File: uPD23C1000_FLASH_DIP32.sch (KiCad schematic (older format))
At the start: 7 parts, among them J1 uPD23C1000 / FLASH, U1 GLS29EE010 (TSOP), U2 SST39SF010 (TSOP), U3 SST39SF010 / GLS29EE010 (PLCC)

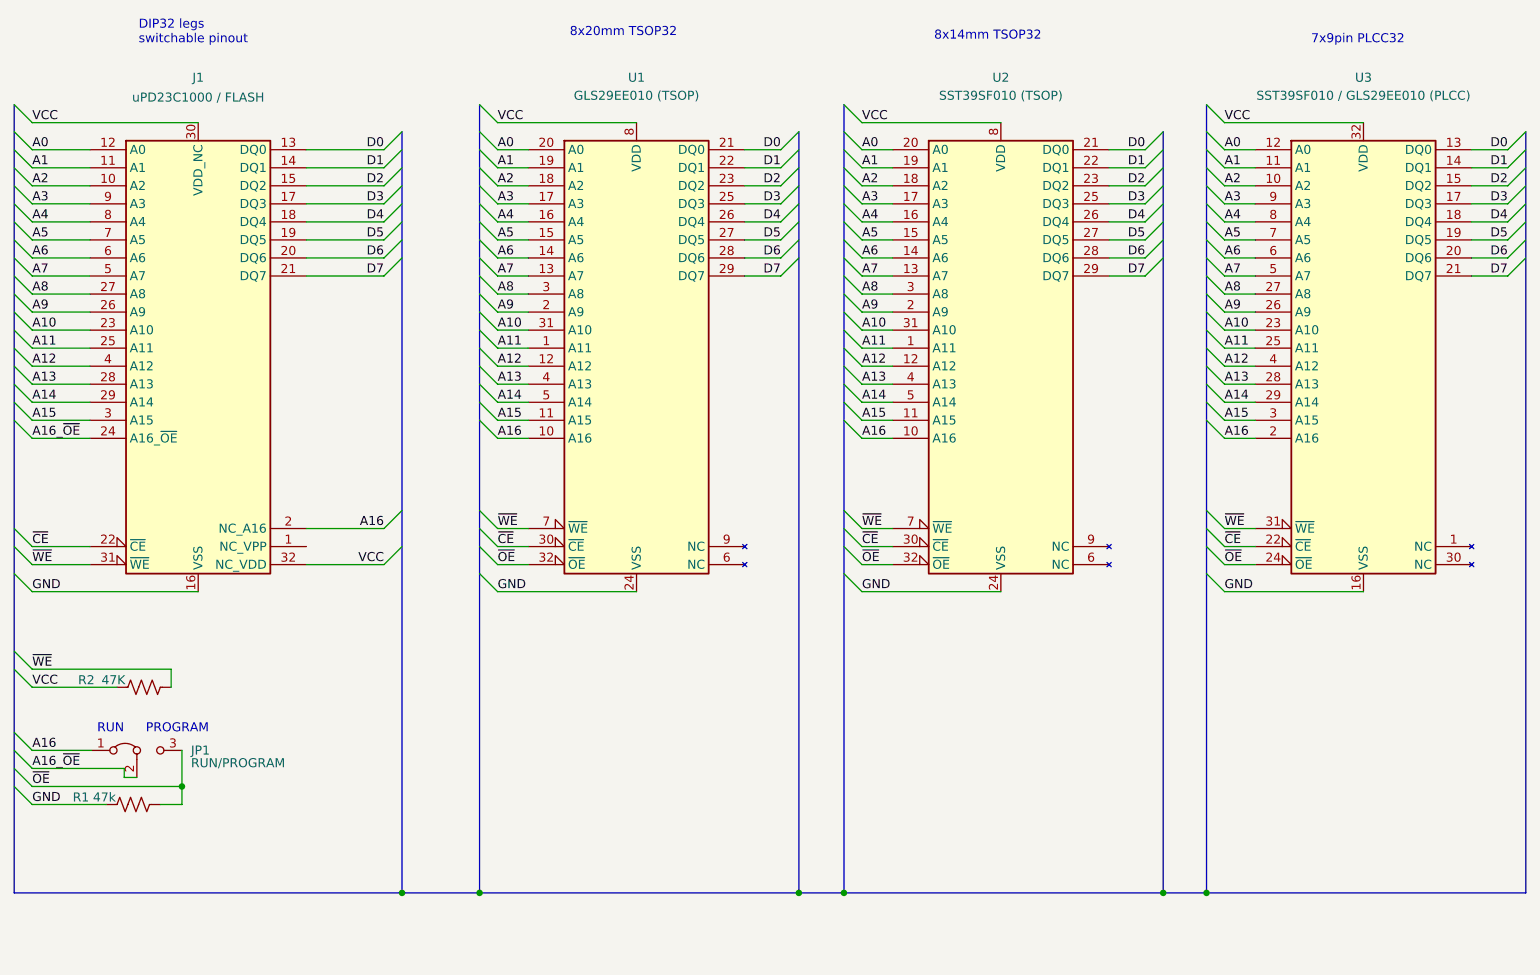
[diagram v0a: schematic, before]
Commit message: docs for FlashROM_8300, add VPP & pullup on FlashROM_8300 to support old flash, eeprom, & eprom devices.
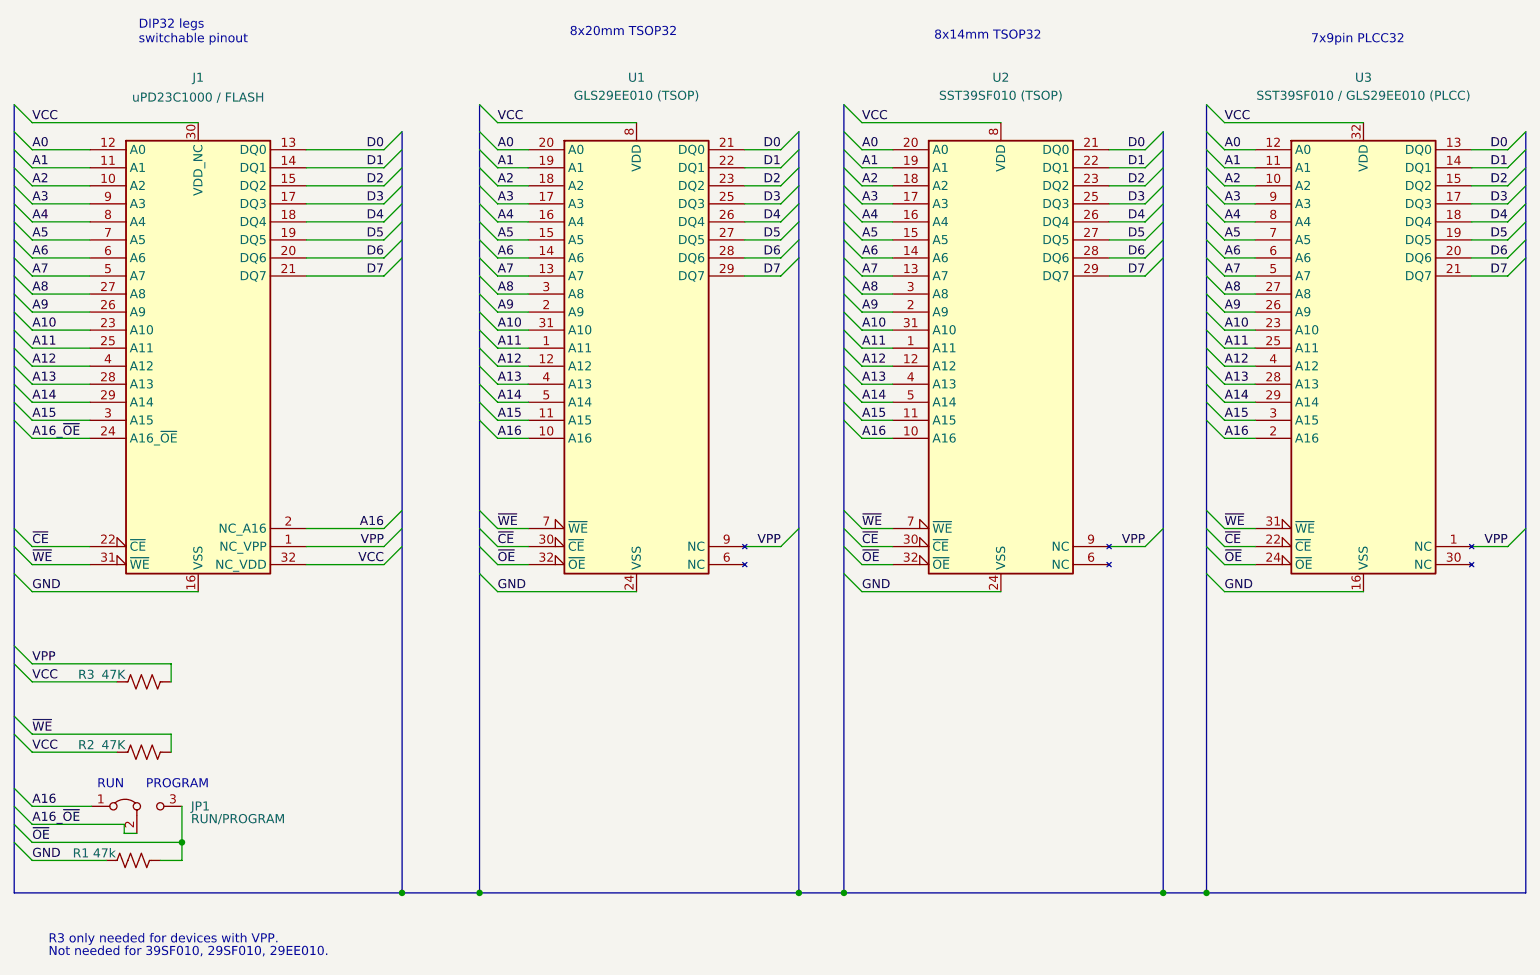
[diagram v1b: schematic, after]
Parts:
- added R3: 47K, 000_LOCAL:R_0805, symbol 000_LOCAL:R_US
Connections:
- net VCC: now also R3.2
- net VPP: now reaches J1.1 (NC_VPP)
- net VPP: now also U1.9 (NC), U2.9 (NC), U3.1 (NC), R3.1
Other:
- note added: "Not needed for 39SF010, 29SF010, 29EE010."
- note added: "R3 only needed for devices with VPP."
- moved on the sheet: JP1, R1, R2
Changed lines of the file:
@@
 Text Label 1270 3900 0    50   ~ 0
 A16_~OE
-Text Label 1270 5930 0    50   ~ 0
+Text Label 1270 6240 0    50   ~ 0
 GND
 Text Label 3850 4500 0    50   ~ 0
@@
 	3750 4400 3850 4500
 Entry Wire Line
-	1170 5830 1270 5930
+	1170 6140 1270 6240
 Entry Wire Line
 	3750 3600 3850 3700
@@
 L 000_LOCAL:R_US R1
 U 1 1 5E614D7E
-P 1830 5930
-F 0 "R1" V 1790 5640 50  0000 C CNN
-F 1 "47k" V 1790 5770 50  0000 C CNN
-F 2 "000_LOCAL:R_0805" V 1870 5920 50  0001 C CNN
-F 3 "~" H 1830 5930 50  0001 C CNN
-	1    1830 5930
+P 1830 6240
+F 0 "R1" V 1790 5950 50  0000 C CNN
+F 1 "47k" V 1790 6080 50  0000 C CNN
+F 2 "000_LOCAL:R_0805" V 1870 6230 50  0001 C CNN
+F 3 "~" H 1830 6240 50  0001 C CNN
+	1    1830 6240
 	0    1    1    0
 $EndComp
@@
 ~OE
 Entry Wire Line
-	1170 5530 1270 5630
-Text Label 1270 5630 0    50   ~ 0
+	1170 5840 1270 5940
+Text Label 1270 5940 0    50   ~ 0
 A16
 Entry Wire Line
-	1170 5080 1270 5180
-Entry Wire Line
-	1170 5180 1270 5280
-Text Label 1270 5280 0    50   ~ 0
+	1170 5440 1270 5540
+Entry Wire Line
+	1170 5540 1270 5640
+Text Label 1270 5640 0    50   ~ 0
 VCC
-Text Label 1270 5180 0    50   ~ 0
+Text Label 1270 5540 0    50   ~ 0
 ~WE
 $Comp
 L Jumper:Jumper_3_Bridged12 JP1
 U 1 1 5E634357
-P 1850 5630
-F 0 "JP1" H 2150 5630 50  0000 L CNN
-F 1 "RUN/PROGRAM" H 2150 5560 50  0000 L CNN
-F 2 "000_LOCAL:Pin_Header_Angled_1x03_Pitch2.54mm" H 1850 5630 50  0001 C CNN
-F 3 "~" H 1850 5630 50  0001 C CNN
-	1    1850 5630
+P 1850 5940
+F 0 "JP1" H 2150 5940 50  0000 L CNN
+F 1 "RUN/PROGRAM" H 2150 5870 50  0000 L CNN
+F 2 "000_LOCAL:Pin_Header_Angled_1x03_Pitch2.54mm" H 1850 5940 50  0001 C CNN
+F 3 "~" H 1850 5940 50  0001 C CNN
+	1    1850 5940
 	1    0    0    -1
 $EndComp
 Wire Wire Line
-	1270 5630 1600 5630
-Entry Wire Line
-	1170 5630 1270 5730
-Entry Wire Line
-	1170 5730 1270 5830
-Wire Wire Line
-	1850 5780 1780 5780
-Wire Wire Line
-	1780 5780 1780 5730
-Wire Wire Line
-	1780 5730 1270 5730
-Wire Wire Line
-	1270 5830 2100 5830
-Wire Wire Line
-	2100 5830 2100 5630
-Text Label 1270 5830 0    50   ~ 0
+	1270 5940 1600 5940
+Entry Wire Line
+	1170 5940 1270 6040
+Entry Wire Line
+	1170 6040 1270 6140
+Wire Wire Line
+	1850 6090 1780 6090
+Wire Wire Line
+	1780 6090 1780 6040
+Wire Wire Line
+	1780 6040 1270 6040
+Wire Wire Line
+	1270 6140 2100 6140
+Wire Wire Line
+	2100 6140 2100 5940
+Text Label 1270 6140 0    50   ~ 0
 ~OE
-Text Label 1270 5730 0    50   ~ 0
+Text Label 1270 6040 0    50   ~ 0
 A16_~OE
 Wire Wire Line
-	1270 5930 1680 5930
-Wire Wire Line
-	1980 5930 2100 5930
-Wire Wire Line
-	2100 5930 2100 5830
-Connection ~ 2100 5830
+	1270 6240 1680 6240
+Wire Wire Line
+	1980 6240 2100 6240
+Wire Wire Line
+	2100 6240 2100 6140
+Connection ~ 2100 6140
 Entry Wire Line
 	3750 4500 3850 4600
@@
 L 000_LOCAL:R_US R2
 U 1 1 5E802DCC
-P 1890 5280
-F 0 "R2" V 1850 4960 50  0000 C CNN
-F 1 "47K" V 1850 5110 50  0000 C CNN
-F 2 "000_LOCAL:R_0805" V 1930 5270 50  0001 C CNN
-F 3 "~" H 1890 5280 50  0001 C CNN
-	1    1890 5280
+P 1890 5640
+F 0 "R2" V 1850 5320 50  0000 C CNN
+F 1 "47K" V 1850 5470 50  0000 C CNN
+F 2 "000_LOCAL:R_0805" V 1930 5630 50  0001 C CNN
+F 3 "~" H 1890 5640 50  0001 C CNN
+	1    1890 5640
 	0    1    1    0
 $EndComp
 Wire Wire Line
-	1270 5280 1740 5280
-Wire Wire Line
-	1270 5180 2040 5180
+	1270 5640 1740 5640
+Wire Wire Line
+	1270 5540 2040 5540
 Text Label 3220 4400 2    50   ~ 0
 A16
@@
 	7780 6420 9550 6420
 Wire Wire Line
-	2040 5280 2040 5180
+	2040 5640 2040 5540
 Wire Wire Line
 	1270 4750 2190 4750
-Text Notes 1630 5540 0    50   ~ 0
+Text Notes 1630 5850 0    50   ~ 0
 RUN
-Text Notes 1900 5540 0    50   ~ 0
+Text Notes 1900 5850 0    50   ~ 0
 PROGRAM
+Entry Wire Line
+	3220 4500 3320 4400
+Wire Wire Line
+	3220 4500 2790 4500
+Text Label 3220 4500 2    50   ~ 0
+VPP
+Entry Wire Line
+	5420 4500 5520 4400
+Wire Wire Line
+	5420 4500 5220 4500
+Text Label 5420 4500 2    50   ~ 0
+VPP
+Entry Wire Line
+	7440 4500 7540 4400
+Wire Wire Line
+	7440 4500 7240 4500
+Text Label 7440 4500 2    50   ~ 0
+VPP
+Entry Wire Line
+	9450 4500 9550 4400
+Wire Wire Line
+	9450 4500 9250 4500
+Text Label 9450 4500 2    50   ~ 0
+VPP
+Entry Wire Line
+	1170 5050 1270 5150
+Entry Wire Line
+	1170 5150 1270 5250
+Text Label 1270 5250 0    50   ~ 0
+VCC
+Text Label 1270 5150 0    50   ~ 0
+VPP
+$Comp
+L 000_LOCAL:R_US R3
+U 1 1 5E74DD94
+P 1890 5250
+F 0 "R3" V 1850 4930 50  0000 C CNN
+F 1 "47K" V 1850 5080 50  0000 C CNN
+F 2 "000_LOCAL:R_0805" V 1930 5240 50  0001 C CNN
+F 3 "~" H 1890 5250 50  0001 C CNN
+	1    1890 5250
+	0    1    1    0
+$EndComp
+Wire Wire Line
+	1270 5250 1740 5250
+Wire Wire Line
+	1270 5150 2040 5150
+Wire Wire Line
+	2040 5250 2040 5150
+Text Notes 1360 6710 0    50   ~ 0
+R3 only needed for devices with VPP.
+Text Notes 1360 6780 0    50   ~ 0
+Not needed for 39SF010, 29SF010, 29EE010.
 Wire Bus Line
 	5520 2200 5520 6420

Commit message: FlexROM_100 programming adapter, FlexROM_102 programming jumpers
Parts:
- JP1: footprint 000_LOCAL:Pin_Header_Angled_1x03_Pitch2.54mm -> 000_LOCAL:Pin_Header_Angled_1x03_Pitch2.54mm_12shorted
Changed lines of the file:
@@
 F 0 "JP1" H 2150 5940 50  0000 L CNN
 F 1 "RUN/PROGRAM" H 2150 5870 50  0000 L CNN
-F 2 "000_LOCAL:Pin_Header_Angled_1x03_Pitch2.54mm" H 1850 5940 50  0001 C CNN
+F 2 "000_LOCAL:Pin_Header_Angled_1x03_Pitch2.54mm_12shorted" H 1850 5940 50  0001 C CNN
 F 3 "~" H 1850 5940 50  0001 C CNN
 	1    1850 5940
